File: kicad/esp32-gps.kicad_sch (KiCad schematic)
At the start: 35 parts, among them J1 Conn_Coaxial_Small, J2 Conn_Coaxial_Small, Q1 BCW66G, Q2 BCW66G, SW1 RESET, SW2 BOOT, U1 ESP32-PICO-V3, U2 GP-01, U3 CP2102N-Axx-xQFN28

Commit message: init
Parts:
- removed J1, J2: Conn_Coaxial_Small, Connector_Coaxial:U.FL_Molex_MCRF_73412-0110_Vertical, symbol Connector:Conn_Coaxial_Small
- added J1, J2: MHF4, PCM_yvolodym:MHF4, symbol PCM_yvolodym:MHF4
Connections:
- net GND: now also J1.2 (GND), J2.2 (GND)
- net at U2.11 (RF): now also J2.1 (SIGNAL)
- net at C3.1, C4.1: now also J1.1 (SIGNAL)
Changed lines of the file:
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@@
 	)
 	(symbol
+		(lib_id "PCM_yvolodym:MHF4")
+		(at 127 147.32 180)
+		(unit 1)
+		(exclude_from_sim no)
+		(in_bom yes)
+		(on_board yes)
+		(dnp no)
+		(fields_autoplaced yes)
+		(property "Reference" "J2"
+			(at 127.5195 140.97 0)
+			(effects
+				(font
+					(size 1.27 1.27)
+				)
+			)
+		)
+		(property "Value" "MHF4"
+			(at 127.5195 143.51 0)
+			(effects
+				(font
+					(size 1.27 1.27)
+				)
+			)
+		)
+		(property "Footprint" "PCM_yvolodym:MHF4"
+			(at 127 147.32 0)
+			(effects
+				(font
+					(size 1.27 1.27)
+				)
+				(hide yes)
+			)
+		)
+		(property "Datasheet" ""
+			(at 127 147.32 0)
+			(effects
+				(font
+					(size 1.27 1.27)
+				)
+				(hide yes)
+			)
+		)
+		(property "Description" "I-PEX MHF4 / MHF4L compatible SMD micro RF coaxial connector receptacle (U.FL-type)"
+			(at 127 147.32 0)
+			(effects
+				(font
+					(size 1.27 1.27)
+				)
+				(hide yes)
+			)
+		)
+		(pin "2"
+		)
+		(pin "1"
+		)
+		(instances
+			(project "esp32-gps"
+				(path "/56168bfe-34bc-4344-8600-222c44ddf088"
+					(reference "J2")
+					(unit 1)
+				)
+			)
+		)
+	)
+	(symbol
 		(lib_id "Mechanical:MountingHole")
 		(at 57.15 161.29 0)
@@
 	)
 	(symbol
-		(lib_id "Connector:Conn_Coaxial_Small")
-		(at 127 147.32 0)
-		(mirror y)
-		(unit 1)
-		(exclude_from_sim no)
-		(in_bom yes)
-		(on_board yes)
-		(dnp no)
-		(property "Reference" "J2"
-			(at 127.5196 140.97 0)
-			(effects
-				(font
-					(size 1.27 1.27)
-				)
-			)
-		)
-		(property "Value" "Conn_Coaxial_Small"
-			(at 127.5196 143.51 0)
-			(effects
-				(font
-					(size 1.27 1.27)
-				)
-			)
-		)
-		(property "Footprint" "Connector_Coaxial:U.FL_Molex_MCRF_73412-0110_Vertical"
-			(at 127 147.32 0)
-			(effects
-				(font
-					(size 1.27 1.27)
-				)
-				(hide yes)
-			)
-		)
-		(property "Datasheet" "~"
-			(at 127 147.32 0)
-			(effects
-				(font
-					(size 1.27 1.27)
-				)
-				(hide yes)
-			)
-		)
-		(property "Description" "small coaxial connector (BNC, SMA, SMB, SMC, Cinch/RCA, LEMO, ...)"
-			(at 127 147.32 0)
-			(effects
-				(font
-					(size 1.27 1.27)
-				)
-				(hide yes)
-			)
-		)
-		(pin "1"
-		)
-		(pin "2"
-		)
-		(instances
-			(project "esp32-gps"
-				(path "/56168bfe-34bc-4344-8600-222c44ddf088"
-					(reference "J2")
-					(unit 1)
-				)
-			)
-		)
-	)
-	(symbol
 		(lib_id "Device:R")
 		(at 113.03 95.25 90)
@@
 	)
 	(symbol
+		(lib_id "PCM_yvolodym:MHF4")
+		(at 64.77 25.4 180)
+		(unit 1)
+		(exclude_from_sim no)
+		(in_bom yes)
+		(on_board yes)
+		(dnp no)
+		(fields_autoplaced yes)
+		(property "Reference" "J1"
+			(at 65.2895 19.05 0)
+			(effects
+				(font
+					(size 1.27 1.27)
+				)
+			)
+		)
+		(property "Value" "MHF4"
+			(at 65.2895 21.59 0)
+			(effects
+				(font
+					(size 1.27 1.27)
+				)
+			)
+		)
+		(property "Footprint" "PCM_yvolodym:MHF4"
+			(at 64.77 25.4 0)
+			(effects
+				(font
+					(size 1.27 1.27)
+				)
+				(hide yes)
+			)
+		)
+		(property "Datasheet" ""
+			(at 64.77 25.4 0)
+			(effects
+				(font
+					(size 1.27 1.27)
+				)
+				(hide yes)
+			)
+		)
+		(property "Description" "I-PEX MHF4 / MHF4L compatible SMD micro RF coaxial connector receptacle (U.FL-type)"
+			(at 64.77 25.4 0)
+			(effects
+				(font
+					(size 1.27 1.27)
+				)
+				(hide yes)
+			)
+		)
+		(pin "2"
+		)
+		(pin "1"
+		)
+		(instances
+			(project "esp32-gps"
+				(path "/56168bfe-34bc-4344-8600-222c44ddf088"
+					(reference "J1")
+					(unit 1)
+				)
+			)
+		)
+	)
+	(symbol
 		(lib_id "Device:C")
 		(at 80.01 35.56 0)
@@
 					(unit 1)
 				)
-			)
-		)
-	)
-	(symbol
-		(lib_id "Connector:Conn_Coaxial_Small")
-		(at 64.77 25.4 0)
-		(mirror y)
-		(unit 1)
-		(exclude_from_sim no)
-		(in_bom yes)
-		(on_board yes)
-		(dnp no)
-		(property "Reference" "J1"
-			(at 65.2896 19.05 0)
-			(effects
-				(font
-					(size 1.27 1.27)
-				)
-			)
-		)
-		(property "Value" "Conn_Coaxial_Small"
-			(at 65.2896 21.59 0)
-			(effects
-				(font
-					(size 1.27 1.27)
-				)
-			)
-		)
-		(property "Footprint" "Connector_Coaxial:U.FL_Molex_MCRF_73412-0110_Vertical"
-			(at 64.77 25.4 0)
-			(effects
-				(font
-					(size 1.27 1.27)
-				)
-				(hide yes)
-			)
-		)
-		(property "Datasheet" "~"
-			(at 64.77 25.4 0)
-			(effects
-				(font
-					(size 1.27 1.27)
-				)
-				(hide yes)
-			)
-		)
-		(property "Description" "small coaxial connector (BNC, SMA, SMB, SMC, Cinch/RCA, LEMO, ...)"
-			(at 64.77 25.4 0)
-			(effects
-				(font
-					(size 1.27 1.27)
-				)
-				(hide yes)
-			)
-		)
-		(pin "1"
-		)
-		(pin "2"
-		)
-		(instances
-			(project "esp32-gps"
-				(path "/56168bfe-34bc-4344-8600-222c44ddf088"
-					(reference "J1")
-					(unit 1)
-				)

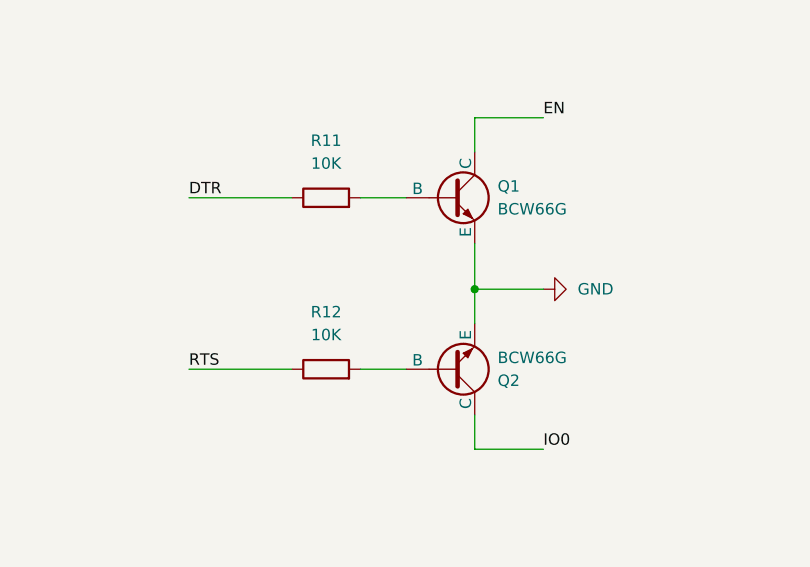
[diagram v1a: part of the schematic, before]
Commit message: shema correction. pcb is not updated
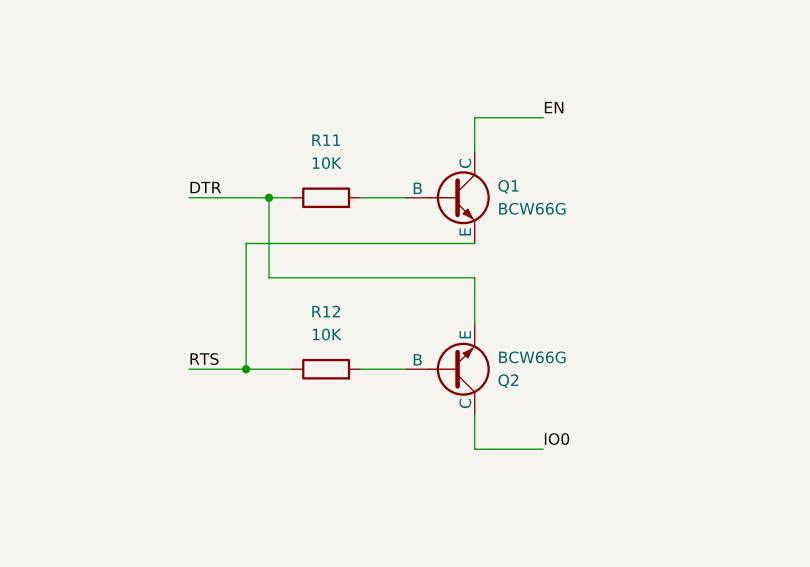
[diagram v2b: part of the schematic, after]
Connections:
- net DTR: now also Q2.3 (E)
- net GND: no longer Q1.3 (E), Q2.3 (E)
- net RTS: now also Q1.3 (E)
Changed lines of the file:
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@@
 	(paper "A4")
 	(junction
-		(at 246.38 132.08)
-		(diameter 0)
-		(color 0 0 0 0)
-	)
-	(junction
 		(at 165.1 147.32)
 		(diameter 0)
@@
 		(color 0 0 0 0)
 	)
+	(junction
+		(at 223.52 121.92)
+		(diameter 0)
+		(color 0 0 0 0)
+	)
+	(junction
+		(at 220.98 140.97)
+		(diameter 0)
+		(color 0 0 0 0)
+	)
 	(no_connect
 		(at 259.08 87.63)
@@
 	(wire
 		(pts
+			(xy 246.38 130.81) (xy 223.52 130.81)
+		)
+		(stroke
+			(width 0)
+			(type default)
+		)
+	)
+	(wire
+		(pts
 			(xy 86.36 62.23) (xy 83.82 62.23)
 		)
@@
 	(wire
 		(pts
-			(xy 214.63 121.92) (xy 226.06 121.92)
+			(xy 214.63 121.92) (xy 223.52 121.92)
 		)
 		(stroke
@@
 	(wire
 		(pts
-			(xy 246.38 132.08) (xy 254 132.08)
+			(xy 220.98 140.97) (xy 226.06 140.97)
 		)
 		(stroke
@@
 	(wire
 		(pts
-			(xy 246.38 127) (xy 246.38 132.08)
+			(xy 220.98 127) (xy 220.98 140.97)
 		)
 		(stroke
@@
 	(wire
 		(pts
-			(xy 246.38 135.89) (xy 246.38 132.08)
+			(xy 30.48 81.28) (xy 43.18 81.28)
 		)
 		(stroke
@@
 	(wire
 		(pts
-			(xy 30.48 81.28) (xy 43.18 81.28)
+			(xy 25.4 69.85) (xy 22.86 69.85)
 		)
 		(stroke
@@
 	(wire
 		(pts
-			(xy 25.4 69.85) (xy 22.86 69.85)
+			(xy 246.38 135.89) (xy 246.38 130.81)
 		)
 		(stroke
@@
 	(wire
 		(pts
+			(xy 223.52 121.92) (xy 226.06 121.92)
+		)
+		(stroke
+			(width 0)
+			(type default)
+		)
+	)
+	(wire
+		(pts
 			(xy 49.53 116.84) (xy 49.53 120.65)
 		)
@@
 	(wire
 		(pts
+			(xy 246.38 127) (xy 220.98 127)
+		)
+		(stroke
+			(width 0)
+			(type default)
+		)
+	)
+	(wire
+		(pts
 			(xy 142.24 144.78) (xy 135.89 144.78)
 		)
@@
 	(wire
 		(pts
+			(xy 223.52 130.81) (xy 223.52 121.92)
+		)
+		(stroke
+			(width 0)
+			(type default)
+		)
+	)
+	(wire
+		(pts
 			(xy 223.52 44.45) (xy 233.68 44.45)
 		)
@@
 	(wire
 		(pts
-			(xy 214.63 140.97) (xy 226.06 140.97)
+			(xy 214.63 140.97) (xy 220.98 140.97)
 		)
 		(stroke
@@
 					(unit 1)
 				)
-			)
-		)
-	)
-	(symbol
-		(lib_id "power:GND")
-		(at 254 132.08 90)
-		(unit 1)
-		(exclude_from_sim no)
-		(in_bom yes)
-		(on_board yes)
-		(dnp no)
-		(fields_autoplaced yes)
-		(property "Reference" "#PWR025"
-			(at 260.35 132.08 0)
-			(effects
-				(font
-					(size 1.27 1.27)
-				)
-				(hide yes)
-			)
-		)
-		(property "Value" "GND"
-			(at 257.81 132.0799 90)
-			(effects
-				(font
-					(size 1.27 1.27)
-				)
-				(justify right)
-			)
-		)
-		(property "Footprint" ""
-			(at 254 132.08 0)
-			(effects
-				(font
-					(size 1.27 1.27)
-				)
-				(hide yes)
-			)
-		)
-		(property "Datasheet" ""
-			(at 254 132.08 0)
-			(effects
-				(font
-					(size 1.27 1.27)
-				)
-				(hide yes)
-			)
-		)
-		(property "Description" "Power symbol creates a global label with name \"GND\" , ground"
-			(at 254 132.08 0)
-			(effects
-				(font
-					(size 1.27 1.27)
-				)
-				(hide yes)
-			)
-		)
-		(pin "1"
-		)
-		(instances
-			(project "esp32-gps"
-				(path "/56168bfe-34bc-4344-8600-222c44ddf088"
-					(reference "#PWR025")
-					(unit 1)
-				)
